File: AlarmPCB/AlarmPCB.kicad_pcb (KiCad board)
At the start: 2 copper layers, 100 x 75 mm, 17 parts

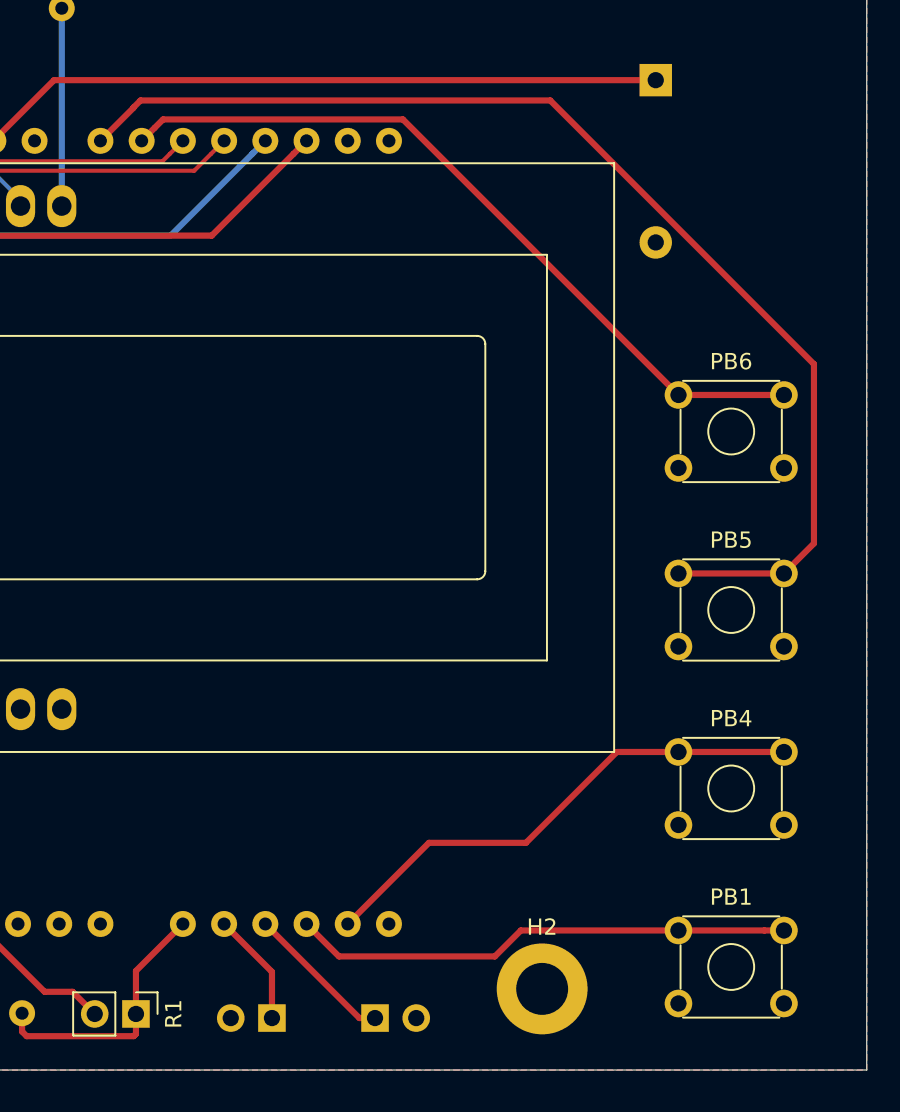
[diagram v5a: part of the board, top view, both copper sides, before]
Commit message: Moved buttons
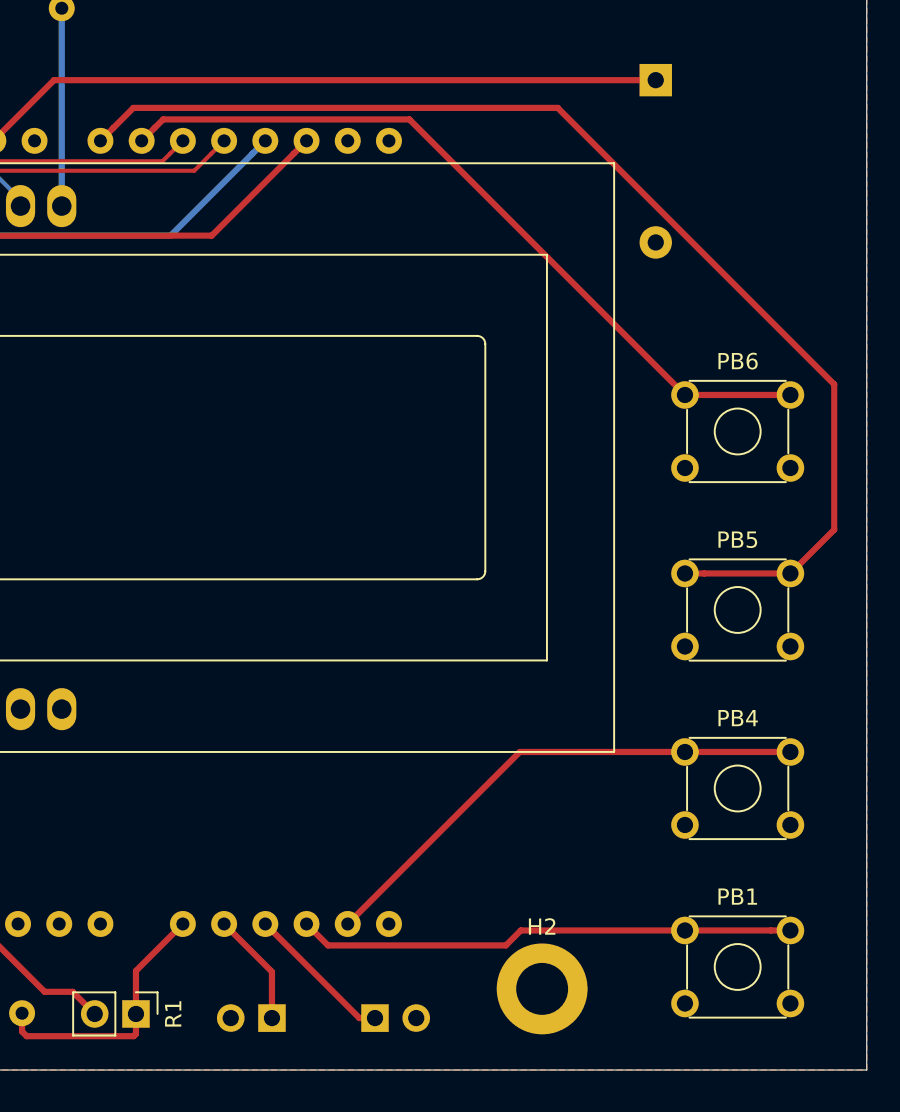
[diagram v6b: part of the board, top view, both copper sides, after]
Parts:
- moved PB1 0.40 mm to (158.8, 156.4)
- moved PB4 0.40 mm to (158.8, 145.4)
- moved PB5 0.40 mm to (158.8, 134.4)
- moved PB6 0.40 mm to (158.8, 123.4)
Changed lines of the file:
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@@
     (thickness 1.6)
     (drawings 22)
-    (tracks 85)
+    (tracks 84)
     (zones 0)
     (modules 17)
@@
   )
   (module ECE:SW_TH_Tactile (layer F.Cu)
-    (at 158.4 134.4)
+    (at 158.8 134.4)
     (descr SW_TH_Tactile_Omron_B3F-10xx_https://www.omron.com/ecb/products/pdf/en-b3f.pdf)
     (tags "Omron B3F-10xx")
@@
   )
   (module ECE:SW_TH_Tactile (layer F.Cu)
-    (at 158.4 123.4)
+    (at 158.8 123.4)
     (descr SW_TH_Tactile_Omron_B3F-10xx_https://www.omron.com/ecb/products/pdf/en-b3f.pdf)
     (tags "Omron B3F-10xx")
@@
   )
   (module ECE:SW_TH_Tactile (layer F.Cu)
-    (at 158.4 145.4)
+    (at 158.8 145.4)
     (descr SW_TH_Tactile_Omron_B3F-10xx_https://www.omron.com/ecb/products/pdf/en-b3f.pdf)
     (tags "Omron B3F-10xx")
@@
   )
   (module ECE:SW_TH_Tactile (layer F.Cu)
-    (at 158.4 156.4)
+    (at 158.8 156.4)
     (descr SW_TH_Tactile_Omron_B3F-10xx_https://www.omron.com/ecb/products/pdf/en-b3f.pdf)
     (tags "Omron B3F-10xx")
@@
     (arrow2b (pts (xy 172 147.25) (xy 171.413579 146.123496)))
   )
-  (dimension 4 (width 0.15) (layer Dwgs.User)
-    (gr_text "4.000 mm" (at 168 173.3) (layer Dwgs.User)
+  (dimension 8 (width 0.15) (layer Dwgs.User)
+    (gr_text "8.000 mm" (at 166 173.3) (layer Dwgs.User)
       (effects (font (size 1 1) (thickness 0.15)))
     )
     (feature1 (pts (xy 170 159) (xy 170 172.586421)))
-    (feature2 (pts (xy 166 159) (xy 166 172.586421)))
-    (crossbar (pts (xy 166 172) (xy 170 172)))
+    (feature2 (pts (xy 162 159) (xy 162 172.586421)))
+    (crossbar (pts (xy 162 172) (xy 170 172)))
     (arrow1a (pts (xy 170 172) (xy 168.873496 172.586421)))
     (arrow1b (pts (xy 170 172) (xy 168.873496 171.413579)))
-    (arrow2a (pts (xy 166 172) (xy 167.126504 172.586421)))
-    (arrow2b (pts (xy 166 172) (xy 167.126504 171.413579)))
+    (arrow2a (pts (xy 162 172) (xy 163.126504 172.586421)))
+    (arrow2b (pts (xy 162 172) (xy 163.126504 171.413579)))
   )
   (dimension 11 (width 0.15) (layer Dwgs.User)
@@
   (gr_line (start 170 165) (end 170 90) (layer Edge.Cuts) (width 0.05))
   (gr_line (start 70 165) (end 170 165) (layer Edge.Cuts) (width 0.05))
-  (segment (start 149 151) (end 154.6 145.4) (width 0.381) (layer F.Cu) (net 6))
-  (segment (start 138.02 156) (end 143.02 151) (width 0.381) (layer F.Cu) (net 6))
-  (segment (start 154.6 145.4) (end 164.9 145.4) (width 0.381) (layer F.Cu) (net 6))
-  (segment (start 143.02 151) (end 149 151) (width 0.381) (layer F.Cu) (net 6))
-  (segment (start 163.697919 156.4) (end 164.9 156.4) (width 0.381) (layer F.Cu) (net 8))
-  (segment (start 148.685658 156.4) (end 163.697919 156.4) (width 0.381) (layer F.Cu) (net 8))
-  (segment (start 147.085658 158) (end 148.685658 156.4) (width 0.381) (layer F.Cu) (net 8))
-  (segment (start 137.48 158) (end 147.085658 158) (width 0.381) (layer F.Cu) (net 8))
-  (segment (start 135.48 156) (end 137.48 158) (width 0.381) (layer F.Cu) (net 8))
+  (segment (start 148.62 145.4) (end 138.02 156) (width 0.381) (layer F.Cu) (net 6))
+  (segment (start 165.3 145.4) (end 148.62 145.4) (width 0.381) (layer F.Cu) (net 6))
+  (segment (start 164.097919 156.4) (end 165.3 156.4) (width 0.381) (layer F.Cu) (net 8))
+  (segment (start 148.685658 156.4) (end 164.097919 156.4) (width 0.381) (layer F.Cu) (net 8))
+  (segment (start 147.765157 157.320501) (end 148.685658 156.4) (width 0.381) (layer F.Cu) (net 8))
+  (segment (start 136.800501 157.320501) (end 147.765157 157.320501) (width 0.381) (layer F.Cu) (net 8))
+  (segment (start 135.48 156) (end 136.800501 157.320501) (width 0.381) (layer F.Cu) (net 8))
   (segment (start 90.136899 111.76) (end 92.646899 109.25) (width 0.254) (layer F.Cu) (net 9))
   (segment (start 89.916 111.76) (end 90.136899 111.76) (width 0.254) (layer F.Cu) (net 9))
@@
   (segment (start 119.92 104) (end 157 104) (width 0.381) (layer F.Cu) (net 15))
   (segment (start 116.18 107.74) (end 119.92 104) (width 0.381) (layer F.Cu) (net 15))
-  (segment (start 125.25 105.25) (end 150.500342 105.25) (width 0.381) (layer F.Cu) (net 18))
-  (segment (start 150.500342 105.25) (end 166.75 121.499658) (width 0.381) (layer F.Cu) (net 18))
-  (segment (start 122.78 107.74) (end 124.811509 105.708491) (width 0.381) (layer F.Cu) (net 18))
-  (segment (start 124.811509 105.708491) (end 124.811509 105.688491) (width 0.381) (layer F.Cu) (net 18))
-  (segment (start 158.4 134.4) (end 164.9 134.4) (width 0.381) (layer F.Cu) (net 18))
-  (segment (start 166.75 121.499658) (end 166.75 132.55) (width 0.381) (layer F.Cu) (net 18))
-  (segment (start 124.811509 105.688491) (end 125.25 105.25) (width 0.381) (layer F.Cu) (net 18))
-  (segment (start 166.75 132.55) (end 164.9 134.4) (width 0.381) (layer F.Cu) (net 18))
-  (segment (start 158.4 123.4) (end 141.419499 106.419499) (width 0.381) (layer F.Cu) (net 19))
-  (segment (start 141.419499 106.419499) (end 126.640501 106.419499) (width 0.381) (layer F.Cu) (net 19))
+  (segment (start 160.002081 134.4) (end 165.3 134.4) (width 0.381) (layer F.Cu) (net 18))
+  (segment (start 158.8 134.4) (end 160.002081 134.4) (width 0.381) (layer F.Cu) (net 18))
+  (segment (start 123.579999 106.940001) (end 122.78 107.74) (width 0.381) (layer F.Cu) (net 18))
+  (segment (start 124.811511 105.708489) (end 123.579999 106.940001) (width 0.381) (layer F.Cu) (net 18))
+  (segment (start 150.958831 105.708489) (end 124.811511 105.708489) (width 0.381) (layer F.Cu) (net 18))
+  (segment (start 168 122.749658) (end 150.958831 105.708489) (width 0.381) (layer F.Cu) (net 18))
+  (segment (start 168 131.7) (end 168 122.749658) (width 0.381) (layer F.Cu) (net 18))
+  (segment (start 165.3 134.4) (end 168 131.7) (width 0.381) (layer F.Cu) (net 18))
+  (segment (start 164.097919 123.4) (end 158.8 123.4) (width 0.381) (layer F.Cu) (net 19))
+  (segment (start 165.3 123.4) (end 164.097919 123.4) (width 0.381) (layer F.Cu) (net 19))
+  (segment (start 126.119999 106.940001) (end 125.32 107.74) (width 0.381) (layer F.Cu) (net 19))
   (segment (start 126.640501 106.419499) (end 126.119999 106.940001) (width 0.381) (layer F.Cu) (net 19))
-  (segment (start 126.119999 106.940001) (end 125.32 107.74) (width 0.381) (layer F.Cu) (net 19))
-  (segment (start 164.9 123.4) (end 158.4 123.4) (width 0.381) (layer F.Cu) (net 19))
+  (segment (start 141.819499 106.419499) (end 126.640501 106.419499) (width 0.381) (layer F.Cu) (net 19))
+  (segment (start 158.8 123.4) (end 141.819499 106.419499) (width 0.381) (layer F.Cu) (net 19))
   (segment (start 115.959999 156.799999) (end 115.16 156) (width 0.381) (layer F.Cu) (net 20))
   (segment (start 119.339499 160.179499) (end 115.959999 156.799999) (width 0.381) (layer F.Cu) (net 20))
